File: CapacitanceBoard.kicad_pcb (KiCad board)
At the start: 2 copper layers, 17.7 x 21.2 mm, 6 parts

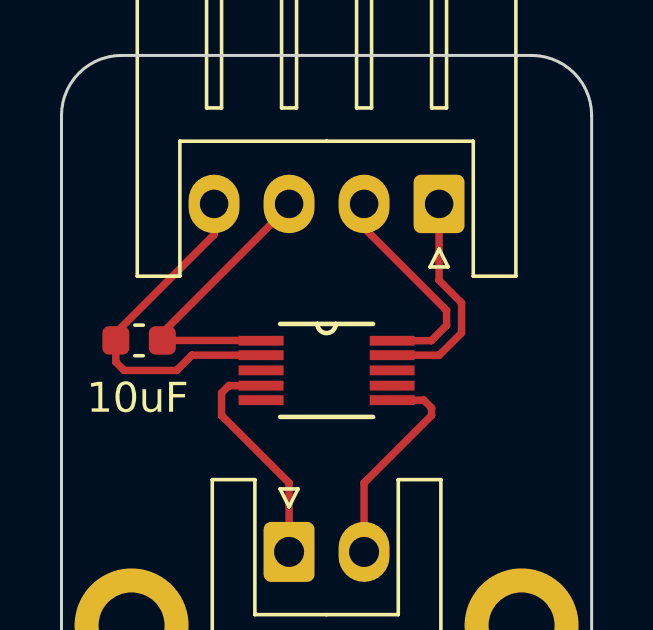
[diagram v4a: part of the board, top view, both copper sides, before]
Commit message: Added Second Decoupling Cap
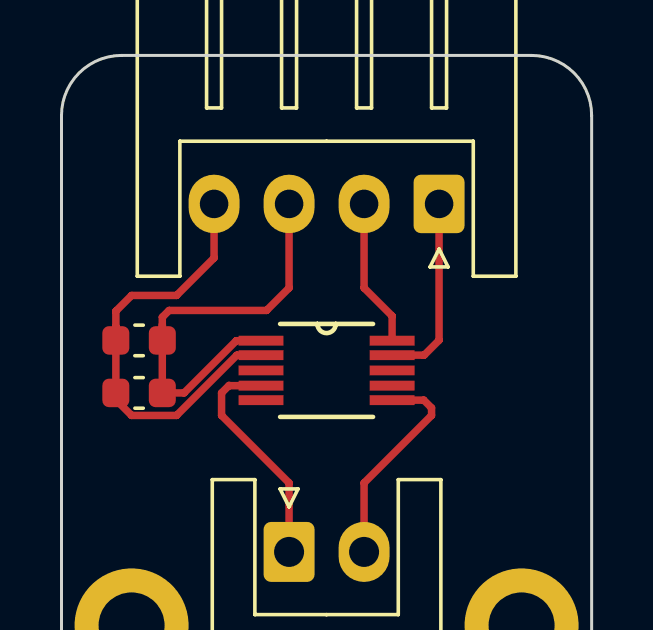
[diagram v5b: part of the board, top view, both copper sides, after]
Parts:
- added REF**: C_0603_1608Metric, Capacitor_SMD:C_0603_1608Metric, F.Cu at (172.8, 123.2)
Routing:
- net (no net): track 50.2 -> 55.4 mm
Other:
- board text removed: "10uF"
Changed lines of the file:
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@@
+    )
+  )
+  (footprint "Capacitor_SMD:C_0603_1608Metric" (layer "F.Cu")
+    (at 172.75 123.25)
+    (descr "Capacitor SMD 0603 (1608 Metric), square (rectangular) end terminal, IPC_7351 nominal, (Body size source: IPC-SM-782 page 76, https://www.pcb-3d.com/wordpress/wp-content/uploads/ipc-sm-782a_amendment_1_and_2.pdf), generated with kicad-footprint-generator")
+    (tags "capacitor")
+    (attr smd)
+    (fp_text reference "REF**" (at 0 -1.43) (layer "F.SilkS") hide
+        (effects (font (size 1 1) (thickness 0.15)))
+    )
+    (fp_text value "C_0603_1608Metric" (at 0 1.43) (layer "F.Fab") hide
+        (effects (font (size 1 1) (thickness 0.15)))
+    )
+    (fp_text user "${REFERENCE}" (at 0 0) (layer "F.Fab")
+        (effects (font (size 0.4 0.4) (thickness 0.06)))
+    )
+    (fp_line (start -0.14058 -0.51) (end 0.14058 -0.51)
+      (stroke (width 0.12) (type solid)) (layer "F.SilkS"))
+    (fp_line (start -0.14058 0.51) (end 0.14058 0.51)
+      (stroke (width 0.12) (type solid)) (layer "F.SilkS"))
+    (fp_line (start -1.48 -0.73) (end 1.48 -0.73)
+      (stroke (width 0.05) (type solid)) (layer "F.CrtYd"))
+    (fp_line (start -1.48 0.73) (end -1.48 -0.73)
+      (stroke (width 0.05) (type solid)) (layer "F.CrtYd"))
+    (fp_line (start 1.48 -0.73) (end 1.48 0.73)
+      (stroke (width 0.05) (type solid)) (layer "F.CrtYd"))
+    (fp_line (start 1.48 0.73) (end -1.48 0.73)
+      (stroke (width 0.05) (type solid)) (layer "F.CrtYd"))
+    (fp_line (start -0.8 -0.4) (end 0.8 -0.4)
+      (stroke (width 0.1) (type solid)) (layer "F.Fab"))
+    (fp_line (start -0.8 0.4) (end -0.8 -0.4)
+      (stroke (width 0.1) (type solid)) (layer "F.Fab"))
+    (fp_line (start 0.8 -0.4) (end 0.8 0.4)
+      (stroke (width 0.1) (type solid)) (layer "F.Fab"))
+    (fp_line (start 0.8 0.4) (end -0.8 0.4)
+      (stroke (width 0.1) (type solid)) (layer "F.Fab"))
+    (pad "1" smd roundrect (at -0.775 0) (size 0.9 0.95) (layers "F.Cu" "F.Paste" "F.Mask") (roundrect_rratio 0.25))
+    (pad "2" smd roundrect (at 0.775 0) (size 0.9 0.95) (layers "F.Cu" "F.Paste" "F.Mask") (roundrect_rratio 0.25))
+    (model "${KICAD6_3DMODEL_DIR}/Capacitor_SMD.3dshapes/C_0603_1608Metric.wrl"
+      (offset (xyz 0 0 0))
+      (scale (xyz 1 1 1))
+      (rotate (xyz 0 0 0))
     )
   )
@@
   (gr_line (start 170.164214 114) (end 170.164214 131.25)
     (stroke (width 0.1) (type default)) (layer "Edge.Cuts"))
-  (gr_text "10uF\n" (at 171 124) (layer "F.SilkS")
-    (effects (font (size 1 1) (thickness 0.15)) (justify left bottom))
-  )
+  (segment (start 177 120.5) (end 177.75 119.75) (width 0.25) (layer "F.Cu") (net 0))
+  (segment (start 171.975 120.525) (end 171.975 121.5) (width 0.25) (layer "F.Cu") (net 0))
   (segment (start 177.75 126.25) (end 175.5 124) (width 0.25) (layer "F.Cu") (net 0))
   (segment (start 180.25 128.55) (end 180.25 126.25) (width 0.25) (layer "F.Cu") (net 0))
   (segment (start 175.758 123.008) (end 176.8156 123.008) (width 0.25) (layer "F.Cu") (net 0))
   (segment (start 182.5 123.75) (end 182.2406 123.4906) (width 0.25) (layer "F.Cu") (net 0))
-  (segment (start 182.742 121.992) (end 181.1844 121.992) (width 0.25) (layer "F.Cu") (net 0))
-  (segment (start 172.25 122.5) (end 174 122.5) (width 0.25) (layer "F.Cu") (net 0))
-  (segment (start 182.4906 121.5094) (end 181.1844 121.5094) (width 0.25) (layer "F.Cu") (net 0))
+  (segment (start 177.75 116.95) (end 177.55 116.95) (width 0.25) (layer "F.Cu") (net 0))
+  (segment (start 172.5 120) (end 171.975 120.525) (width 0.25) (layer "F.Cu") (net 0))
+  (segment (start 181.1844 120.6844) (end 181.1844 121.5094) (width 0.25) (layer "F.Cu") (net 0))
+  (segment (start 171.975 123.475) (end 172.5 124) (width 0.25) (layer "F.Cu") (net 0))
   (segment (start 177.75 128.55) (end 177.75 126.25) (width 0.25) (layer "F.Cu") (net 0))
-  (segment (start 182.75 122) (end 182.742 121.992) (width 0.25) (layer "F.Cu") (net 0))
   (segment (start 176.8062 121.5) (end 176.8156 121.5094) (width 0.25) (layer "F.Cu") (net 0))
   (segment (start 175.5 123.25) (end 175.75 123) (width 0.25) (layer "F.Cu") (net 0))
-  (segment (start 180.25 116.95) (end 180.25 117.75) (width 0.25) (layer "F.Cu") (net 0))
-  (segment (start 175.25 116.95) (end 175.25 117.975) (width 0.25) (layer "F.Cu") (net 0))
-  (segment (start 171.975 121.5) (end 171.975 122.225) (width 0.25) (layer "F.Cu") (net 0))
+  (segment (start 172.5 124) (end 174 124) (width 0.25) (layer "F.Cu") (net 0))
+  (segment (start 171.975 123.25) (end 171.975 123.475) (width 0.25) (layer "F.Cu") (net 0))
+  (segment (start 182.25 121.992) (end 181.1844 121.992) (width 0.25) (layer "F.Cu") (net 0))
+  (segment (start 174 120) (end 172.5 120) (width 0.25) (layer "F.Cu") (net 0))
   (segment (start 182.2406 123.4906) (end 181.1844 123.4906) (width 0.25) (layer "F.Cu") (net 0))
-  (segment (start 171.975 122.225) (end 172.25 122.5) (width 0.25) (layer "F.Cu") (net 0))
-  (segment (start 183.5 121.25) (end 182.75 122) (width 0.25) (layer "F.Cu") (net 0))
-  (segment (start 175.25 117.975) (end 171.975 121.25) (width 0.25) (layer "F.Cu") (net 0))
+  (segment (start 171.975 121.5) (end 171.975 123.25) (width 0.25) (layer "F.Cu") (net 0))
   (segment (start 182.5 124) (end 182.5 123.75) (width 0.25) (layer "F.Cu") (net 0))
+  (segment (start 171.975 121.025) (end 171.975 121.25) (width 0.25) (layer "F.Cu") (net 0))
   (segment (start 175.75 123) (end 175.758 123.008) (width 0.25) (layer "F.Cu") (net 0))
-  (segment (start 177.75 116.95) (end 177.75 117.025) (width 0.25) (layer "F.Cu") (net 0))
-  (segment (start 174 122.5) (end 174.508 121.992) (width 0.25) (layer "F.Cu") (net 0))
-  (segment (start 182.75 116.95) (end 182.75 119.5) (width 0.25) (layer "F.Cu") (net 0))
-  (segment (start 183.5 120.25) (end 183.5 121.25) (width 0.25) (layer "F.Cu") (net 0))
-  (segment (start 180.25 117.75) (end 183 120.5) (width 0.25) (layer "F.Cu") (net 0))
+  (segment (start 174.25 123.25) (end 175.9906 121.5094) (width 0.25) (layer "F.Cu") (net 0))
+  (segment (start 173.525 120.725) (end 173.75 120.5) (width 0.25) (layer "F.Cu") (net 0))
+  (segment (start 175.25 116.95) (end 175.25 118.75) (width 0.25) (layer "F.Cu") (net 0))
+  (segment (start 177.75 119.75) (end 177.75 116.95) (width 0.25) (layer "F.Cu") (net 0))
+  (segment (start 182.75 121.492) (end 182.25 121.992) (width 0.25) (layer "F.Cu") (net 0))
+  (segment (start 173.525 120.975) (end 173.525 121.25) (width 0.25) (layer "F.Cu") (net 0))
+  (segment (start 176.008 121.992) (end 176.8156 121.992) (width 0.25) (layer "F.Cu") (net 0))
   (segment (start 175.5 124) (end 175.5 123.25) (width 0.25) (layer "F.Cu") (net 0))
   (segment (start 180.25 126.25) (end 182.5 124) (width 0.25) (layer "F.Cu") (net 0))
-  (segment (start 174.508 121.992) (end 176.8156 121.992) (width 0.25) (layer "F.Cu") (net 0))
-  (segment (start 182.75 119.5) (end 183.5 120.25) (width 0.25) (layer "F.Cu") (net 0))
-  (segment (start 183 121) (end 182.4906 121.5094) (width 0.25) (layer "F.Cu") (net 0))
-  (segment (start 183 120.5) (end 183 121) (width 0.25) (layer "F.Cu") (net 0))
-  (segment (start 177.75 117.025) (end 173.525 121.25) (width 0.25) (layer "F.Cu") (net 0))
-  (segment (start 173.525 121.5) (end 176.8062 121.5) (width 0.25) (layer "F.Cu") (net 0))
+  (segment (start 173.75 120.5) (end 177 120.5) (width 0.25) (layer "F.Cu") (net 0))
+  (segment (start 173.525 121.5) (end 173.525 120.725) (width 0.25) (layer "F.Cu") (net 0))
+  (segment (start 175.25 118.75) (end 174 120) (width 0.25) (layer "F.Cu") (net 0))
+  (segment (start 180.25 116.95) (end 180.25 119.75) (width 0.25) (layer "F.Cu") (net 0))
+  (segment (start 173.525 121.5) (end 173.525 123.25) (width 0.25) (layer "F.Cu") (net 0))
+  (segment (start 175.9906 121.5094) (end 176.8156 121.5094) (width 0.25) (layer "F.Cu") (net 0))
+  (segment (start 173.525 123.25) (end 174.25 123.25) (width 0.25) (layer "F.Cu") (net 0))
+  (segment (start 174 124) (end 176.008 121.992) (width 0.25) (layer "F.Cu") (net 0))
+  (segment (start 180.25 119.75) (end 181.1844 120.6844) (width 0.25) (layer "F.Cu") (net 0))
+  (segment (start 182.75 116.95) (end 182.75 121.492) (width 0.25) (layer "F.Cu") (net 0))
 )

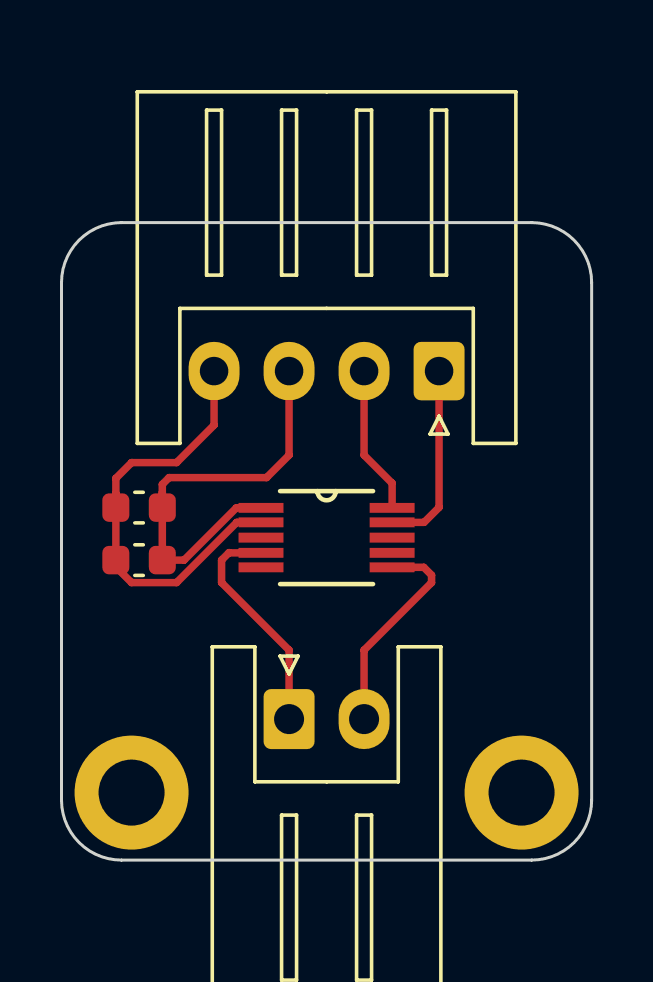
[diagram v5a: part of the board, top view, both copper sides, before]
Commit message: Added Pull-Up Resistors.
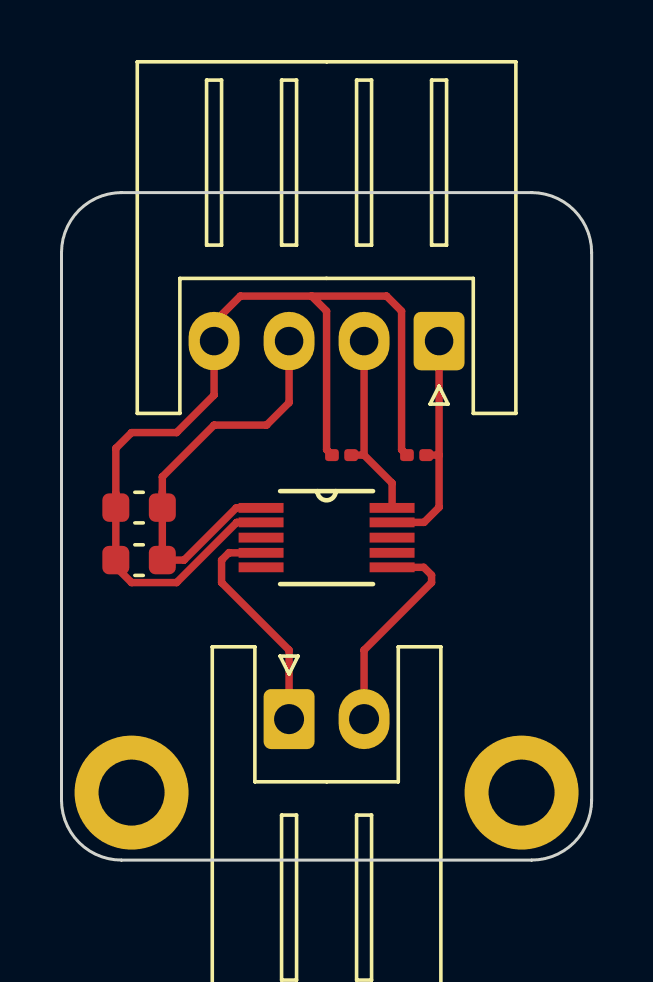
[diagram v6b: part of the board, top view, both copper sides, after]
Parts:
- added REF**: R_0201_0603Metric, Resistor_SMD:R_0201_0603Metric, F.Cu at (182.0, 119.8)
- added REF**: R_0201_0603Metric, Resistor_SMD:R_0201_0603Metric, F.Cu at (179.5, 119.8)
- moved REF** 1.00 mm to (182.8, 116.0)
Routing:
- net (no net): track 55.4 -> 77.3 mm
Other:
- board size 17.7 x 21.2 mm -> 17.7 x 22.2 mm

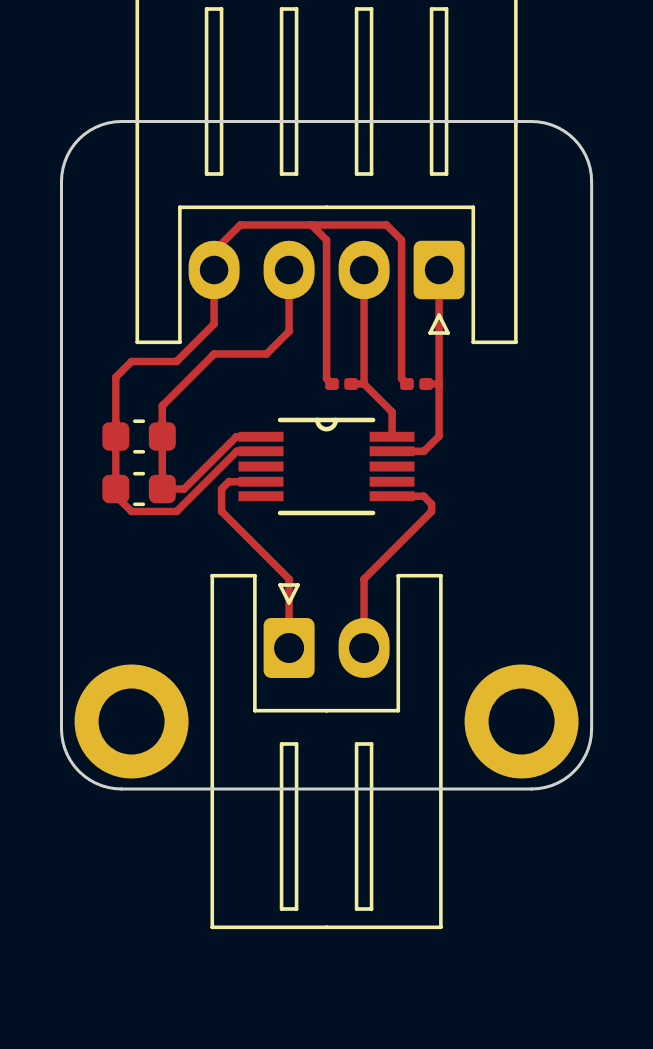
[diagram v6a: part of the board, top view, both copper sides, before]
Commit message: Added EMI Filtering.
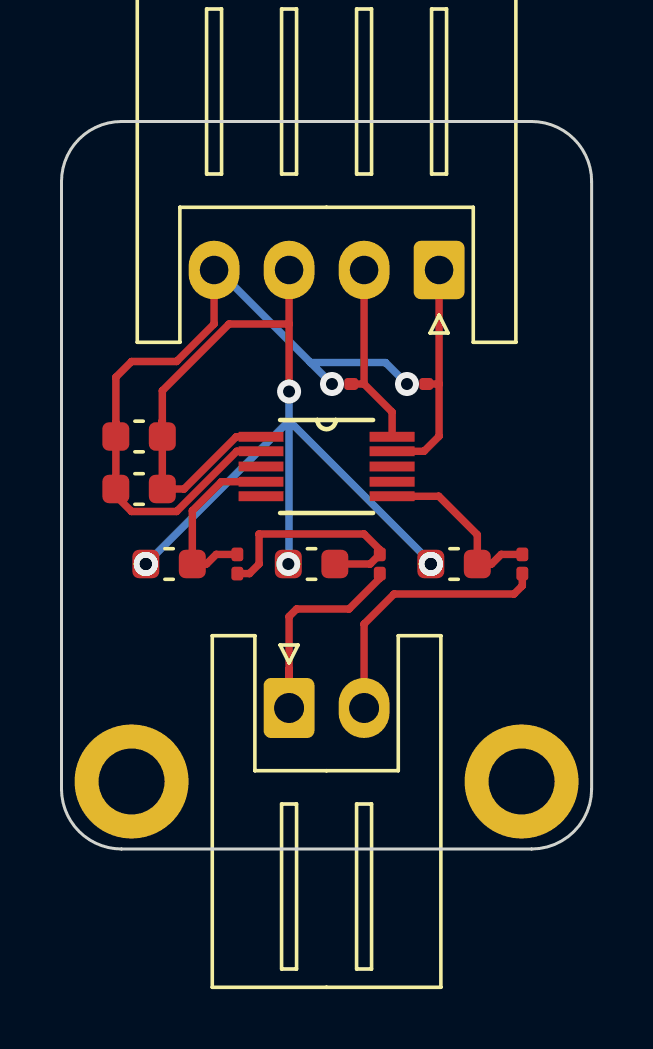
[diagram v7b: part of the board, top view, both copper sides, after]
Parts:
- added REF**: R_0201_0603Metric, Resistor_SMD:R_0201_0603Metric, F.Cu at (176.0, 125.8)
- added REF**: C_0603_1608Metric, Capacitor_SMD:C_0603_1608Metric, F.Cu at (183.2, 125.8)
- added REF**: R_0201_0603Metric, Resistor_SMD:R_0201_0603Metric, F.Cu at (185.5, 125.8)
- added REF**: R_0201_0603Metric, Resistor_SMD:R_0201_0603Metric, F.Cu at (180.8, 125.8)
- added REF**: C_0603_1608Metric, Capacitor_SMD:C_0603_1608Metric, F.Cu at (173.8, 125.8)
- added REF**: C_0603_1608Metric, Capacitor_SMD:C_0603_1608Metric, F.Cu at (178.5, 125.8)
- moved REF** 2.00 mm to (177.8, 130.6)
- moved REF** 2.00 mm to (185.5, 133.0)
- moved REF** 2.00 mm to (172.5, 133.0)
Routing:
- net (no net): track 77.3 -> 114.0 mm, vias 0 -> 8
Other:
- board size 17.7 x 22.2 mm -> 17.7 x 24.2 mm
- board text added: "Capacitive Fill Board"
